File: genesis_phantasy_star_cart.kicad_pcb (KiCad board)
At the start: 4 copper layers, 92.6 x 63.7 mm, 14 parts, among them J1 Sega_MegaDrive_Cart_Conn, J2 Batt, U1 315-5235, U2 MPR-11711, U3 MB8464A-15LL-SK, U4 BQ2201SN

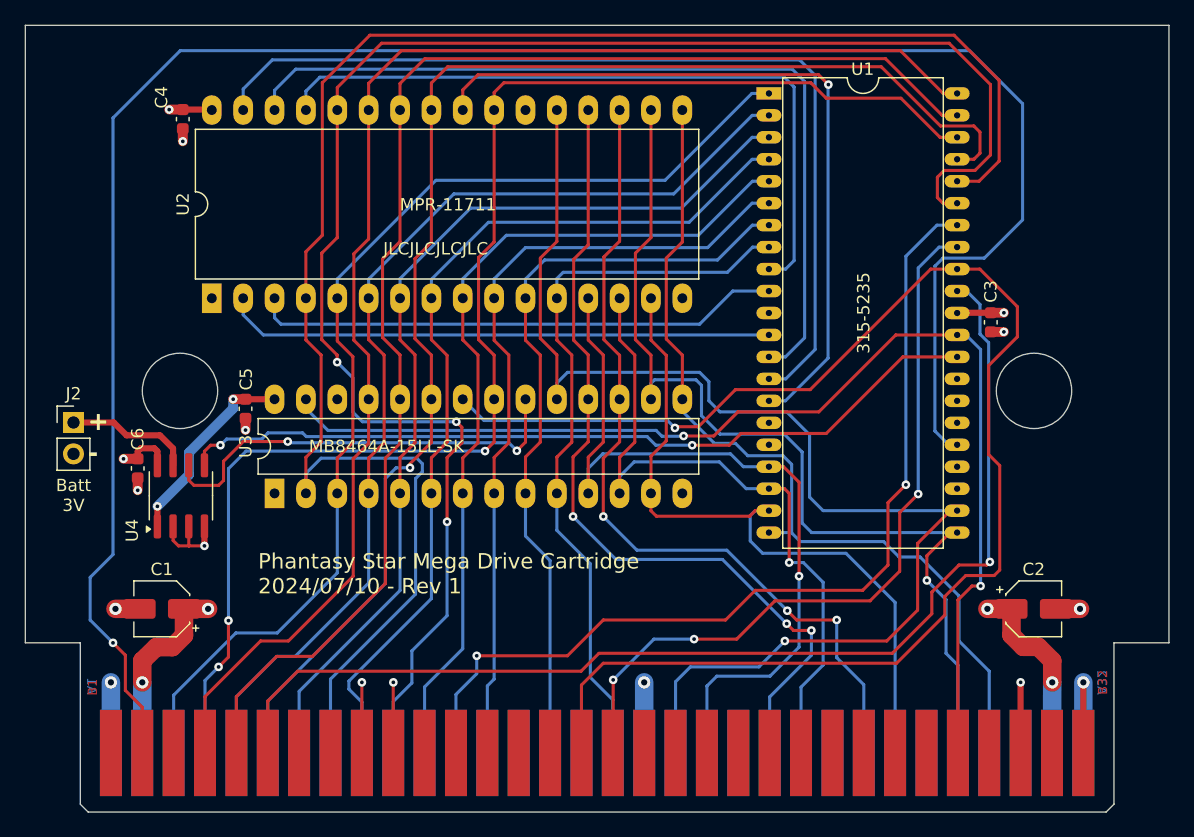
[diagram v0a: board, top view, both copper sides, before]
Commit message: Add 3d model for mapper
* Added 3D model for the U1 mapper chip
* Added an extra +5v and GND via to C1 and C2.
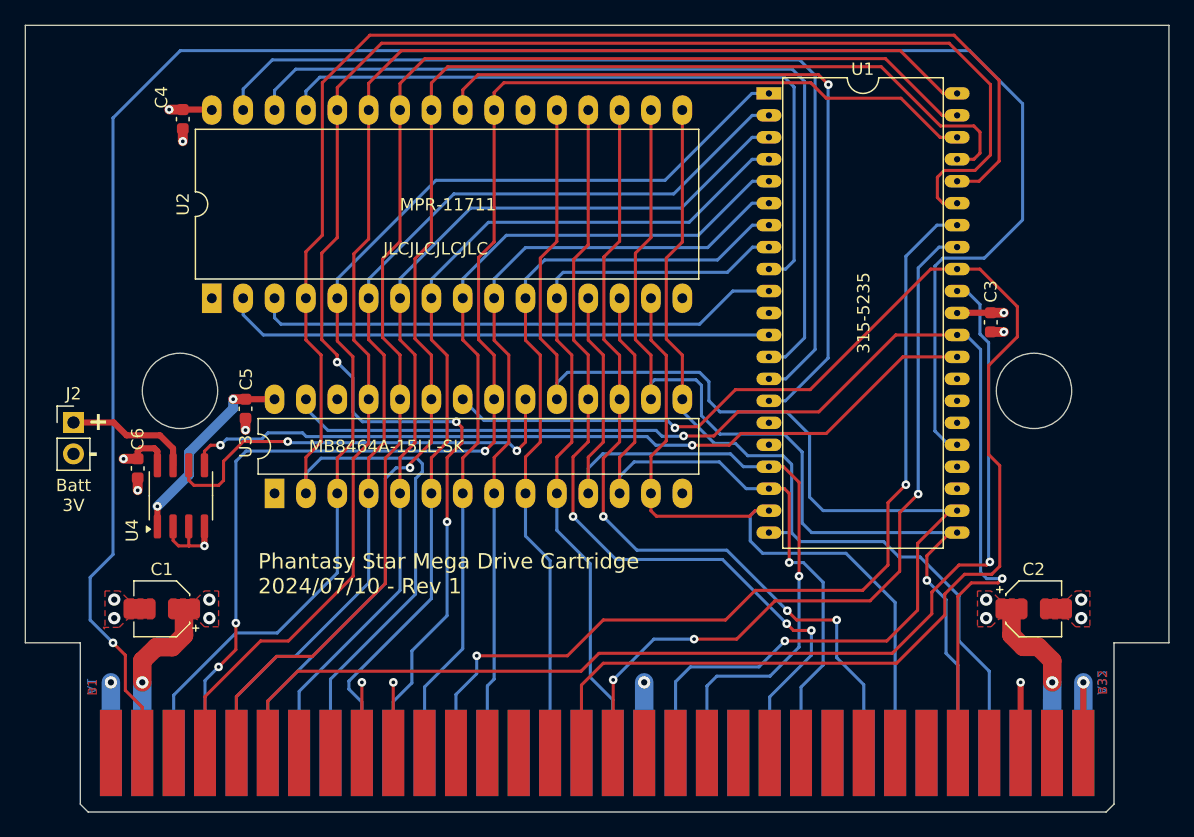
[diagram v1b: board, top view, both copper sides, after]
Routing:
- net GND: track 49.3 -> 45.4 mm, vias 12 -> 14
- net +5V: track 49.1 -> 45.2 mm, vias 8 -> 10
- net /C_~{WR}: track 94.6 -> 97.6 mm
- added copper zone on F.Cu, net +5V
- added copper zone on F.Cu, net GND

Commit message: Rename mapper footprint and model
* Renamed footprint and model for mapper to be more accurate and with
  the dimentions in metric.
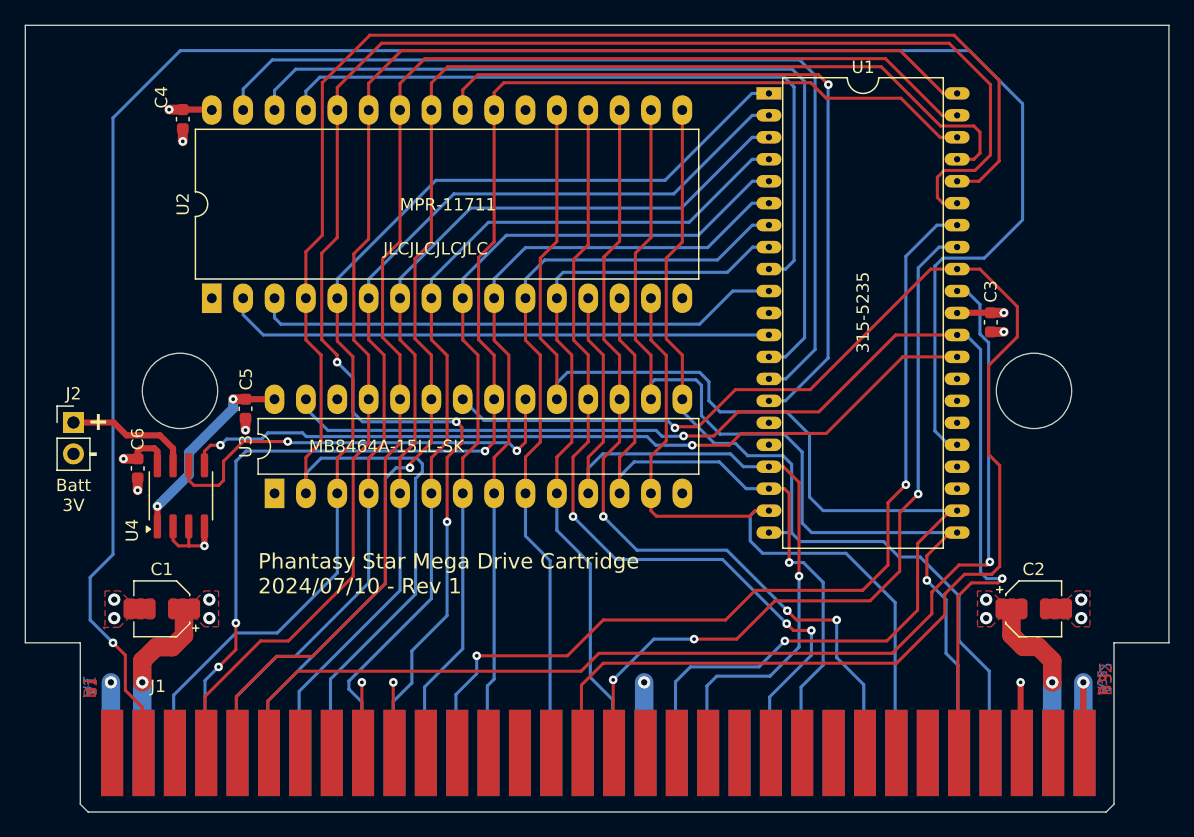
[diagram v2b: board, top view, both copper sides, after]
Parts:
- J1: footprint My_Library:2x32_P2.54mm_Edge -> Custom:2x32_P2.54mm_Edge
- U1: footprint Custom:DIL42_600mil_P70mil_SmallDrill -> Custom:SPDIP-42_W15.24mm_P1.78mm

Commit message: Changes leading to Rev 2 of the board
* Trimmed wings off of the edges of the board to make it a regular
  shape.
* Slightly moved around U1/2/3 to make more room around the cutouts.
* Moved backup battery connection, but remains pin headers as a CR2032
  footprint won't fit on the board with the ICs where they are.
* Enlarged drill size for U1 pads to allow the pins to fit easier.
* Various tracks nudged or rerouted to create more clearance.
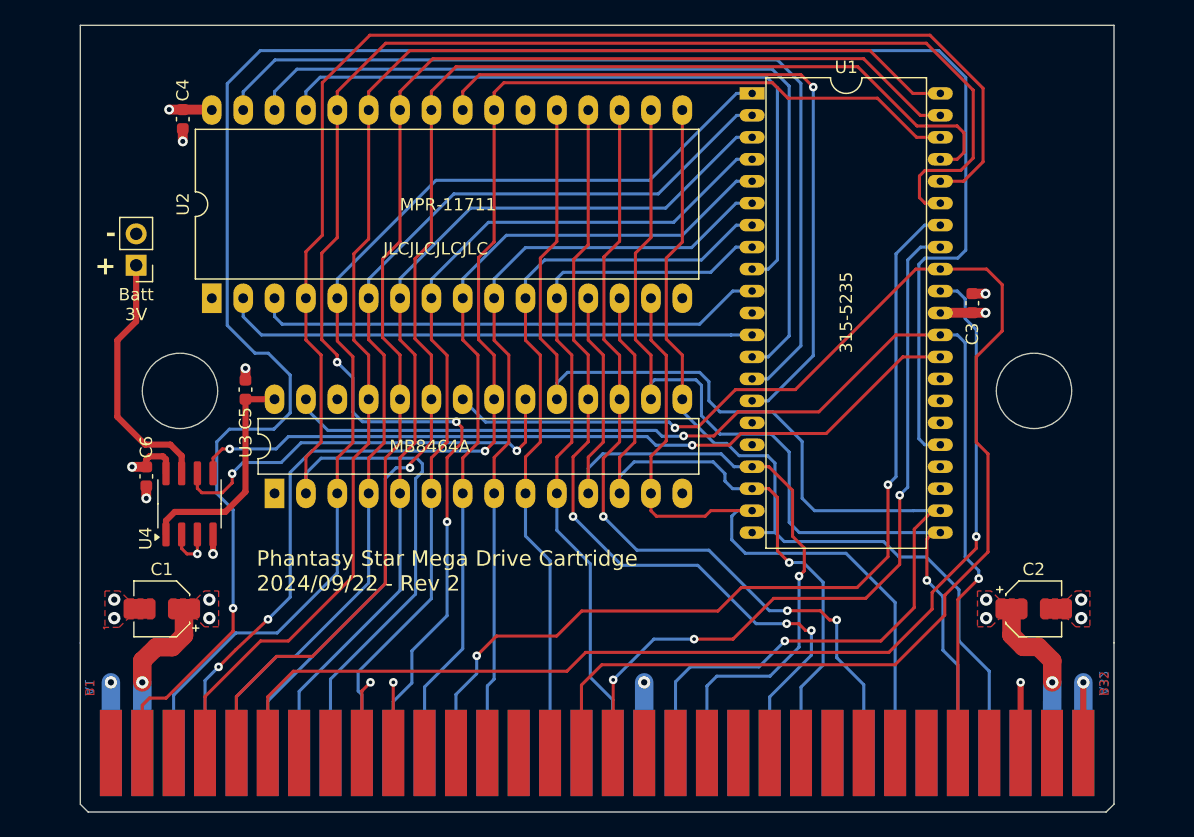
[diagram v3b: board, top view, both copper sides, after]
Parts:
- removed REF**: OSHW-Symbol_6.7x6mm_SilkScreen, Symbol:OSHW-Symbol_6.7x6mm_SilkScreen
- removed REF**: KiCad-Logo2_5mm_SilkScreen, Symbol:KiCad-Logo2_5mm_SilkScreen
- U3: value MB8464A-15LL-SK -> MB8464A
- moved J2 13.7 mm to (72.6, 79.2), turned to 180 degrees
- moved C3 2.16 mm to (140.3, 82.3), turned to 90 degrees
- moved C5 1.55 mm to (81.5, 89.3), turned to 90 degrees
- moved U1 1.36 mm to (122.5, 65.3)
- moved C6 0.95 mm to (73.4, 96.3)
- moved U4 0.95 mm to (76.9, 98.5)
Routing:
- net /BATT+: track 10.3 -> 20.8 mm
- net /C_~{WR}: track 97.6 -> 93.1 mm
- net /C_A10: track 115.2 -> 110.8 mm
- net /C_~{RESET}: track 165.3 -> 162.0 mm
- net /C_D7: track 104.6 -> 102.2 mm
- net /SRAM_{VCC}: track 16.2 -> 18.4 mm, vias 2 -> 0
- net /C_A4: track 74.0 -> 72.0 mm
- net /~{SR_MGMT_{CE}}: track 66.1 -> 64.1 mm
- net /C_D4: track 80.8 -> 78.9 mm
- net /C_~{RD}: track 119.2 -> 117.2 mm
- net /C_A8: track 112.2 -> 110.4 mm
- net /C_A9: track 110.4 -> 108.7 mm
- net /C_A11: track 112.4 -> 110.7 mm
- net /A18: track 76.4 -> 74.8 mm
- net /C_A12: track 141.6 -> 140.0 mm
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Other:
- board size 92.6 x 63.7 mm -> 83.7 x 63.7 mm
- board text added: "Phantasy Star Mega Drive Cartridge 2024/09/22 - Rev 2"
- board text removed: "A1"
- board text removed: "A32"
- board text removed: "B1"
- board text removed: "B32"
- board text removed: "Phantasy Star Mega Drive Cartridge 2024/07/10 - Rev 1"

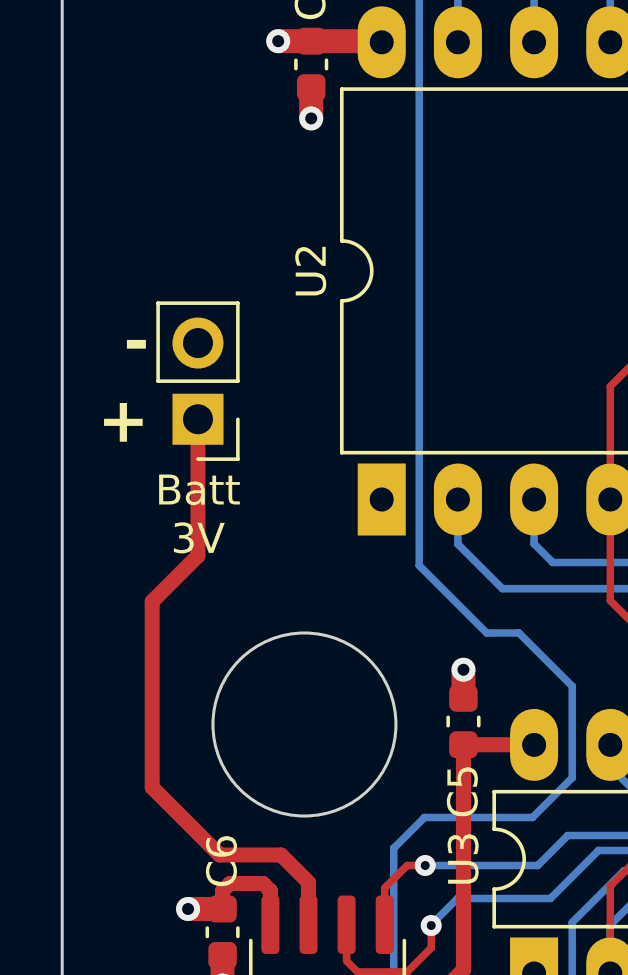
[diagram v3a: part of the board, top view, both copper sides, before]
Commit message: Add NPTH for potential use by battery wires
* Added NPTH for battery wires to use for front soldering. Possible
  stress relief for the wires.
* Rotated battery pin headers to orient better with NPTH.
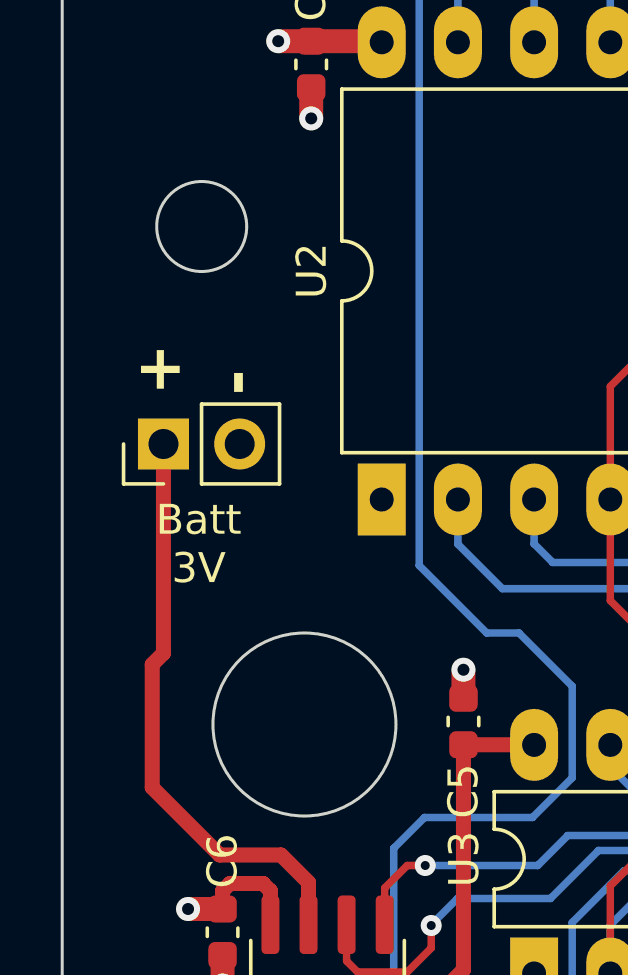
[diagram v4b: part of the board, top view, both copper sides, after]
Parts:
- moved J2 1.42 mm to (71.5, 80.0), turned to 90 degrees
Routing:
- net /BATT+: track 20.8 -> 19.5 mm
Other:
- outline, holes or cut-outs redrawn
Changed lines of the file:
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@@
 	(footprint "Connector_PinHeader_2.54mm:PinHeader_1x02_P2.54mm_Vertical"
 		(layer "F.Cu")
-		(at 72.625 79.225 180)
+		(at 71.475 80.05 90)
 		(descr "Through hole straight pin header, 1x02, 2.54mm pitch, single row")
 		(tags "Through hole pin header THT 1x02 2.54mm single row")
 		(property "Reference" "J2"
-			(at 0 -2.33 0)
+			(at 0 -2.33 90)
 			(layer "F.SilkS")
 			(hide yes)
@@
 		)
 		(property "Value" "Batt"
-			(at 0 4.87 0)
+			(at 0 4.87 90)
 			(layer "F.Fab")
 			(hide yes)
@@
 		)
 		(property "Footprint" "Connector_PinHeader_2.54mm:PinHeader_1x02_P2.54mm_Vertical"
-			(at 0 0 180)
+			(at 0 0 90)
 			(unlocked yes)
 			(layer "F.Fab")
@@
 		)
 		(property "Datasheet" ""
-			(at 0 0 180)
+			(at 0 0 90)
 			(unlocked yes)
 			(layer "F.Fab")
@@
 		)
 		(property "Description" "Generic connector, single row, 01x02, script generated"
-			(at 0 0 180)
+			(at 0 0 90)
 			(unlocked yes)
 			(layer "F.Fab")
@@
 		(attr through_hole dnp)
 		(fp_line
-			(start 1.33 1.270001)
-			(end 1.33 3.87)
+			(start -1.33 -1.33)
+			(end 0 -1.33)
 			(stroke
 				(width 0.12)
@@
 		)
 		(fp_line
-			(start -1.33 3.87)
-			(end 1.33 3.87)
+			(start -1.33 0)
+			(end -1.33 -1.33)
 			(stroke
 				(width 0.12)
@@
 		)
 		(fp_line
-			(start -1.33 1.270001)
-			(end 1.33 1.270001)
+			(start 1.33 1.270001)
+			(end 1.33 3.87)
 			(stroke
 				(width 0.12)
@@
 		(fp_line
 			(start -1.33 1.270001)
-			(end -1.33 3.87)
+			(end 1.33 1.270001)
 			(stroke
 				(width 0.12)
@@
 		)
 		(fp_line
-			(start -1.33 0)
-			(end -1.33 -1.33)
+			(start -1.33 1.270001)
+			(end -1.33 3.87)
 			(stroke
 				(width 0.12)
@@
 		)
 		(fp_line
-			(start -1.33 -1.33)
-			(end 0 -1.33)
+			(start -1.33 3.87)
+			(end 1.33 3.87)
 			(stroke
 				(width 0.12)
@@
 		)
 		(fp_line
-			(start 1.8 4.35)
-			(end 1.8 -1.8)
+			(start 1.8 -1.8)
+			(end -1.8 -1.8)
 			(stroke
 				(width 0.05)
@@
 		)
 		(fp_line
-			(start 1.8 -1.8)
-			(end -1.8 -1.8)
+			(start -1.8 -1.8)
+			(end -1.8 4.35)
 			(stroke
 				(width 0.05)
@@
 		)
 		(fp_line
-			(start -1.8 4.35)
-			(end 1.8 4.35)
+			(start 1.8 4.35)
+			(end 1.8 -1.8)
 			(stroke
 				(width 0.05)
@@
 		)
 		(fp_line
-			(start -1.8 -1.8)
-			(end -1.8 4.35)
+			(start -1.8 4.35)
+			(end 1.8 4.35)
 			(stroke
 				(width 0.05)
@@
 		)
 		(fp_line
-			(start 1.27 3.81)
-			(end -1.27 3.81)
+			(start 1.27 -1.27)
+			(end 1.27 3.81)
 			(stroke
 				(width 0.1)
@@
 		)
 		(fp_line
-			(start 1.27 -1.27)
-			(end 1.27 3.81)
+			(start -0.635 -1.27)
+			(end 1.27 -1.27)
 			(stroke
 				(width 0.1)
@@
 		)
 		(fp_line
-			(start -0.635 -1.27)
-			(end 1.27 -1.27)
+			(start -1.27 -0.635)
+			(end -0.635 -1.27)
 			(stroke
 				(width 0.1)
@@
 		)
 		(fp_line
-			(start -1.27 3.81)
-			(end -1.27 -0.635)
+			(start 1.27 3.81)
+			(end -1.27 3.81)
 			(stroke
 				(width 0.1)
@@
 		)
 		(fp_line
-			(start -1.27 -0.635)
-			(end -0.635 -1.27)
+			(start -1.27 3.81)
+			(end -1.27 -0.635)
 			(stroke
 				(width 0.1)
@@
 		)
 		(fp_text user "${REFERENCE}"
-			(at 0 1.270001 90)
+			(at 0 1.270001 360)
 			(layer "F.Fab")
 			(effects
@@
 		)
 		(pad "1" thru_hole rect
-			(at 0 0 180)
+			(at 0 0 90)
 			(size 1.7 1.7)
 			(drill 1)
@@
 		)
 		(pad "2" thru_hole oval
-			(at 0 2.54 180)
+			(at 0 2.54 90)
 			(size 1.7 1.7)
 			(drill 1)
@@
 		(layer "Edge.Cuts")
 	)
+	(gr_circle
+		(center 72.75 72.8)
+		(end 74.25 72.8)
+		(stroke
+			(width 0.1)
+			(type default)
+		)
+		(fill none)
+		(layer "Edge.Cuts")
+	)
 	(gr_line
 		(start 68.1 109.8)
@@
 	)
 	(gr_text "-"
-		(at 71 75.95 180)
+		(at 74.75 78.425 90)
 		(layer "F.SilkS")
 		(effects
@@
 	)
 	(gr_text "Batt\n3V"
-		(at 72.625 83.8 0)
+		(at 72.65 84.775 0)
 		(layer "F.SilkS")
 		(effects
@@
 	)
 	(gr_text "+"
-		(at 71 78.5 180)
+		(at 72.2 78.425 90)
 		(layer "F.SilkS")
 		(effects
@@
 	)
 	(segment
-		(start 72.625 83.775)
-		(end 72.625 79.225)
+		(start 71.475 87.025)
+		(end 71.475 80.05)
 		(width 0.5)
 		(layer "F.Cu")
@@
 	)
 	(segment
-		(start 71.1 85.3)
-		(end 72.625 83.775)
+		(start 73.35 93.75)
+		(end 71.1 91.5)
 		(width 0.5)
 		(layer "F.Cu")
@@
 	)
 	(segment
-		(start 71.1 91.5)
-		(end 71.1 85.3)
+		(start 71.1 87.4)
+		(end 71.475 87.025)
 		(width 0.5)
 		(layer "F.Cu")
@@
 	)
 	(segment
-		(start 75.395 93.75)
-		(end 73.35 93.75)
+		(start 76.31 94.665)
+		(end 75.395 93.75)
 		(width 0.5)
 		(layer "F.Cu")
@@
 	)
 	(segment
-		(start 73.35 93.75)
-		(end 71.1 91.5)
+		(start 76.31 96.075)
+		(end 76.31 94.665)
 		(width 0.5)
 		(layer "F.Cu")
@@
 	)
 	(segment
-		(start 76.31 94.665)
-		(end 75.395 93.75)
+		(start 75.395 93.75)
+		(end 73.35 93.75)
 		(width 0.5)
 		(layer "F.Cu")
@@
 	)
 	(segment
-		(start 76.31 96.075)
-		(end 76.31 94.665)
+		(start 71.1 91.5)
+		(end 71.1 87.4)
 		(width 0.5)
 		(layer "F.Cu")
@@
 			)
 		)
+	)
+	(zone
+		(net 0)
+		(net_name "")
+		(layers "F.Cu" "In1.Cu" "In2.Cu" "B.Cu")
+		(hatch edge 0.5)
+		(connect_pads
+			(clearance 0)
+		)
+		(min_thickness 0.25)
+		(filled_areas_thickness no)
+		(keepout
+			(tracks not_allowed)
+			(vias not_allowed)
+			(pads not_allowed)
+			(copperpour not_allowed)
+			(footprints not_allowed)
+		)
+		(fill
+			(thermal_gap 0.5)
+			(thermal_bridge_width 0.5)
+		)
+		(polygon
+			(pts
+				(xy 74.45 72.8) (xy 74.431012 72.546628) (xy 74.374474 72.298916) (xy 74.281647 72.062398) (xy 74.154606 71.842356)
+				(xy 73.996188 71.643706) (xy 73.809933 71.470886) (xy 73.6 71.327757) (xy 73.37108 71.217515) (xy 73.128286 71.142623)
+				(xy 72.877041 71.104754) (xy 72.622959 71.104754) (xy 72.371714 71.142623) (xy 72.12892 71.217515)
+				(xy 71.9 71.327757) (xy 71.690067 71.470886) (xy 71.503812 71.643706) (xy 71.345394 71.842356) (xy 71.218353 72.062398)
+				(xy 71.125526 72.298916) (xy 71.068988 72.546628) (xy 71.05 72.8) (xy 71.068988 73.053372) (xy 71.125526 73.301084)
+				(xy 71.218353 73.537602) (xy 71.345394 73.757644) (xy 71.503812 73.956294) (xy 71.690067 74.129114)
+				(xy 71.9 74.272243) (xy 72.12892 74.382485) (xy 72.371714 74.457377) (xy 72.622959 74.495246) (xy 72.877041 74.495246)
+				(xy 73.128286 74.457377) (xy 73.37108 74.382485) (xy 73.6 74.272243) (xy 73.809933 74.129114) (xy 73.996188 73.956294)
+				(xy 74.154606 73.757644) (xy 74.281647 73.537602) (xy 74.374474 73.301084) (xy 74.431012 73.053372)
+				(xy 74.45 72.8)
+			)
+		)
